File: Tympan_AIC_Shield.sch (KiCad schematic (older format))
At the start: 47 parts, among them J1 SJ-3523-SMT-TR, J2 SJ-3524-SMT-TR-PI, P1 CONN_01X06, P2 CONN_01X06, P3 CONN_01X06, P4 CONN_01X06, P5 CONN_01X06, U2 TLV320AIC3206IRSBT, U3 74LVC1G66

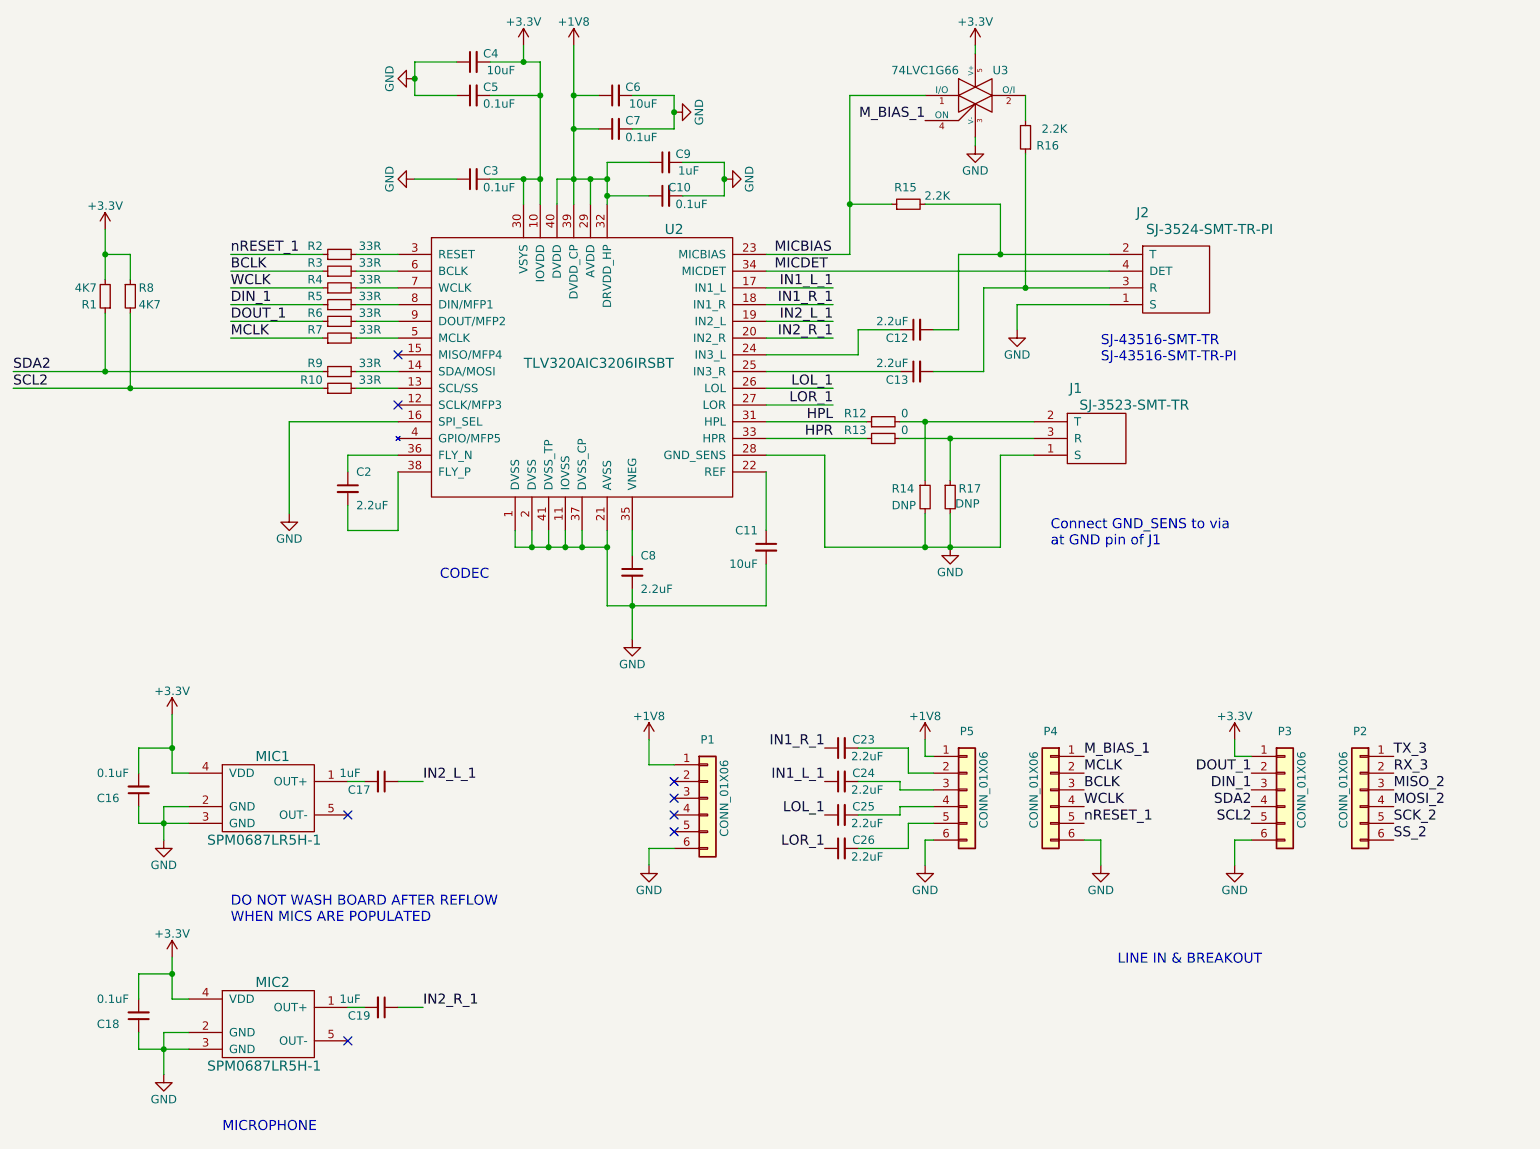
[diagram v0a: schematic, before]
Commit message: Cleaned silk. Need to breakout PDM connections
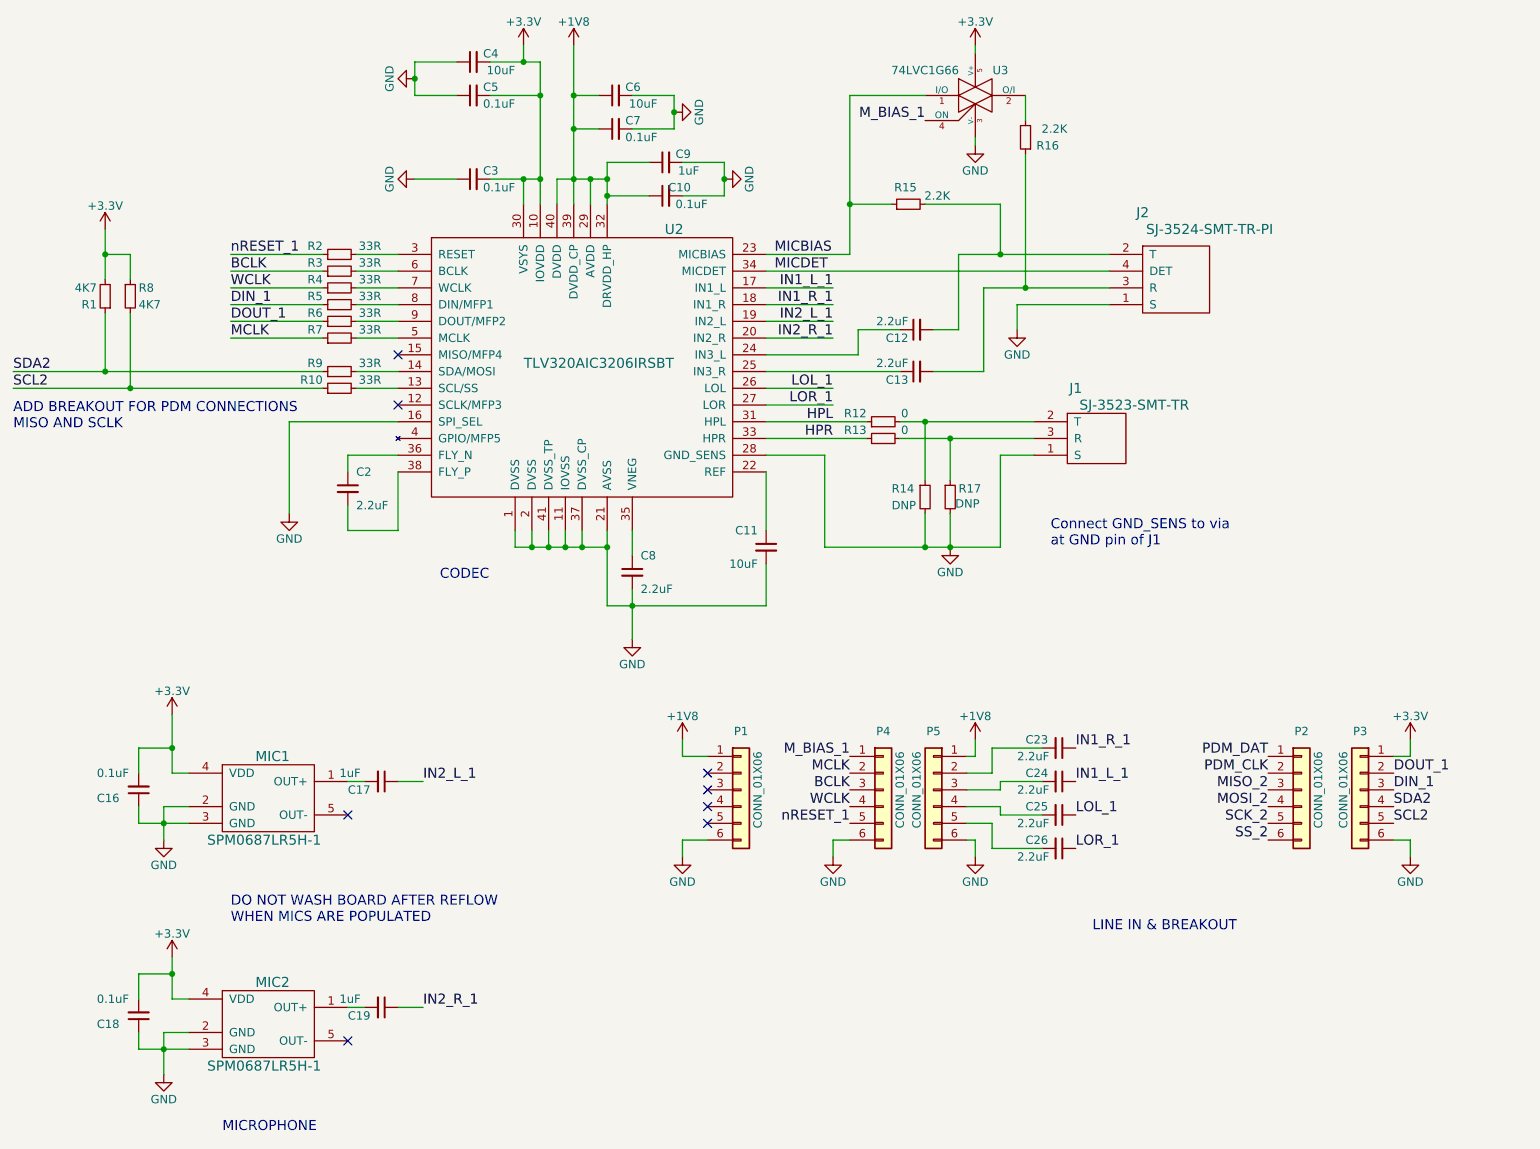
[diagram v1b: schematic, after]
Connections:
- net RX_3 renamed PDM_CLK
- net TX_3 renamed PDM_DAT
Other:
- note added: "ADD BREAKOUT FOR PDM CONNECTIONS\nMISO AND SCLK"
- note removed: "SJ-43516-SMT-TR\nSJ-43516-SMT-TR-PI"
- moved on the sheet: C23, C24, C25, C26, P1, P2, P3, P4, P5

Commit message: added PDM breakout
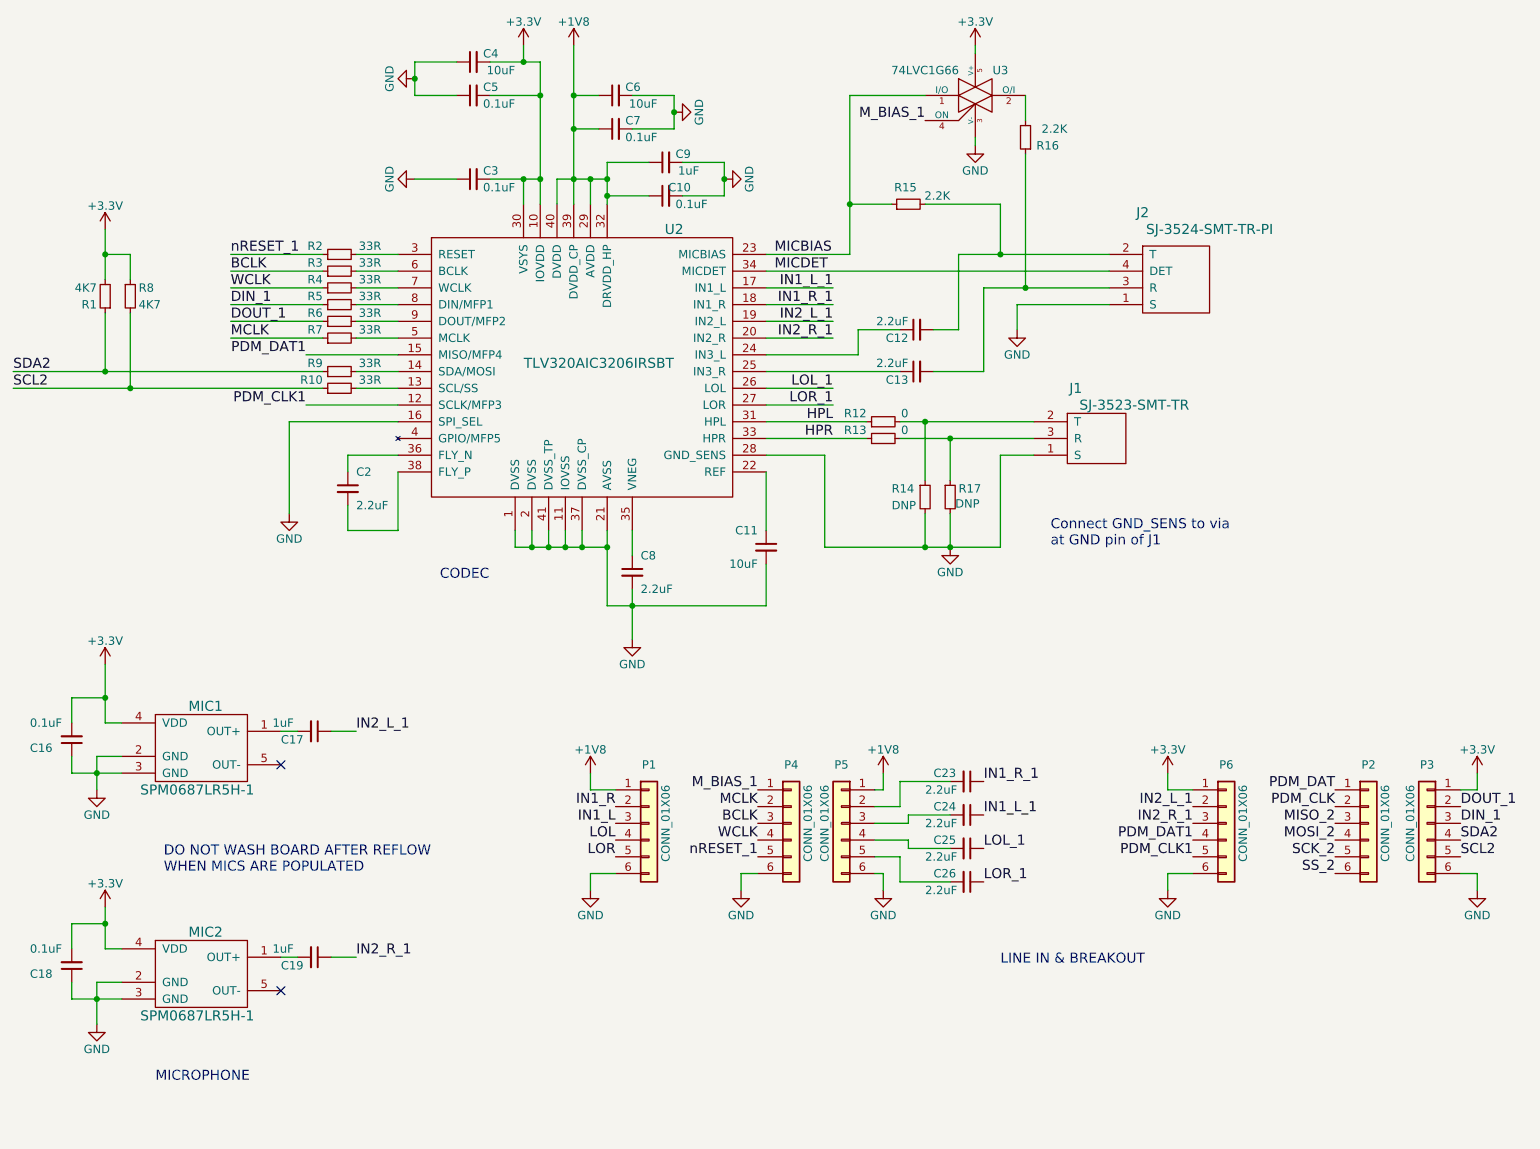
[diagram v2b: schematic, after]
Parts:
- added P6: CONN_01X06, Pin_Headers:Pin_Header_Straight_1x06_Pitch2.54mm, symbol Connector_Generic:Conn_01x06
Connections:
- net +3V3: now also P6.1 (Pin_1)
- net GND: now also P6.6 (Pin_6)
- net IN2_L_1: now also P6.2 (Pin_2)
- net IN2_R_1: now also P6.3 (Pin_3)
- net PDM_CLK1: now reaches U2.12 (SCLK/MFP3)
- net PDM_CLK1: now also P6.5 (Pin_5)
- net PDM_DAT1: now reaches U2.15 (MISO/MFP4)
- net PDM_DAT1: now also P6.4 (Pin_4)
- net IN1_R: now reaches P1.2 (Pin_2)
- net IN1_L: now reaches P1.3 (Pin_3)
- net LOL: now reaches P1.4 (Pin_4)
- net LOR: now reaches P1.5 (Pin_5)
- no-connect marks 8 -> 2
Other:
- note removed: "ADD BREAKOUT FOR PDM CONNECTIONS\nMISO AND SCLK"
- moved on the sheet: C16, C17, C18, C19, C23, C24, C25, C26, MIC1, MIC2, P1, P2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
